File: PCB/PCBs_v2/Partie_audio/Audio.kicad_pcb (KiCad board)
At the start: 2 copper layers, 29.8 x 31.8 mm, 24 parts, among them J1 Conn_01x11, J2 Conn_01x02, U1 PTAS2780RYAR

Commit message: MAJ PCB audio
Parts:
- J1: value Conn_01x11 -> Conn_01x13; footprint Connector_PinHeader_2.00mm:PinHeader_1x11_P2.00mm_Vertical -> Connector_PinHeader_2.00mm:PinHeader_1x13_P2.00mm_Vertical
- moved C2 10.3 mm to (193.6, 39.0)
- moved R1 2.31 mm to (191.6, 46.2)
- moved R2 1.91 mm to (191.0, 43.5), turned to 180 degrees
- moved C4 1.74 mm to (188.5, 48.8)
- moved C10 0.90 mm to (184.8, 40.6)
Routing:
- net GND: track 76.6 -> 12.6 mm, vias 77 -> 74
- net VSNSN: track 19.2 -> 15.4 mm
- net VSNSP: track 17.2 -> 14.0 mm
- net OUTN: track 24.5 -> 21.4 mm
- net /VSNSP_: track 11.1 -> 9.06 mm
- net /VSNSN_: track 4.96 -> 6.78 mm
- net SDIN: track 18.7 -> 16.9 mm
- net SDA: track 15.7 -> 13.9 mm
- net OUTP: track 7.52 -> 9.27 mm
- net /BST_N: track 3.96 -> 5.35 mm
- net +1.8V: track 26.2 -> 27.3 mm
- net /DREG: track 2.84 -> 3.74 mm
- net SBCLK: track 17.6 -> 16.9 mm

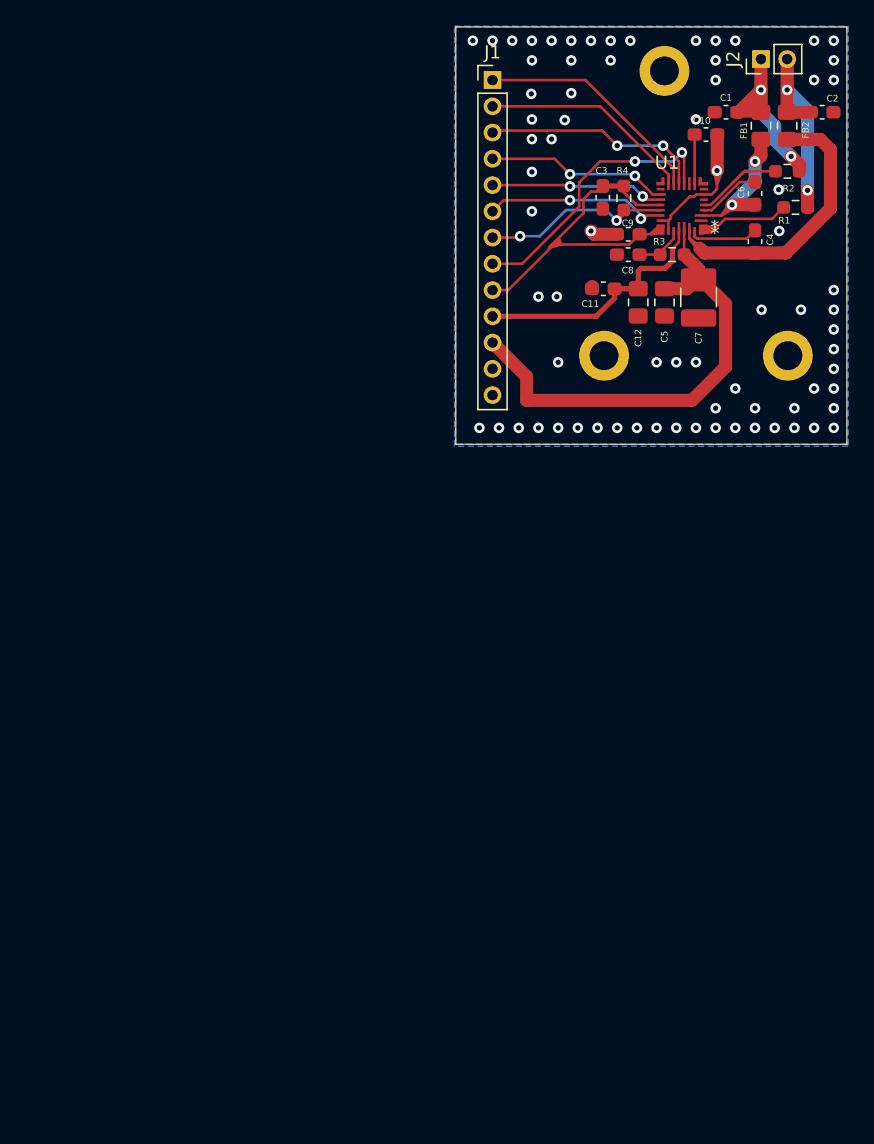
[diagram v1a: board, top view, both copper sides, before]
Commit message: Modification du schéma et du routage de la partie audio
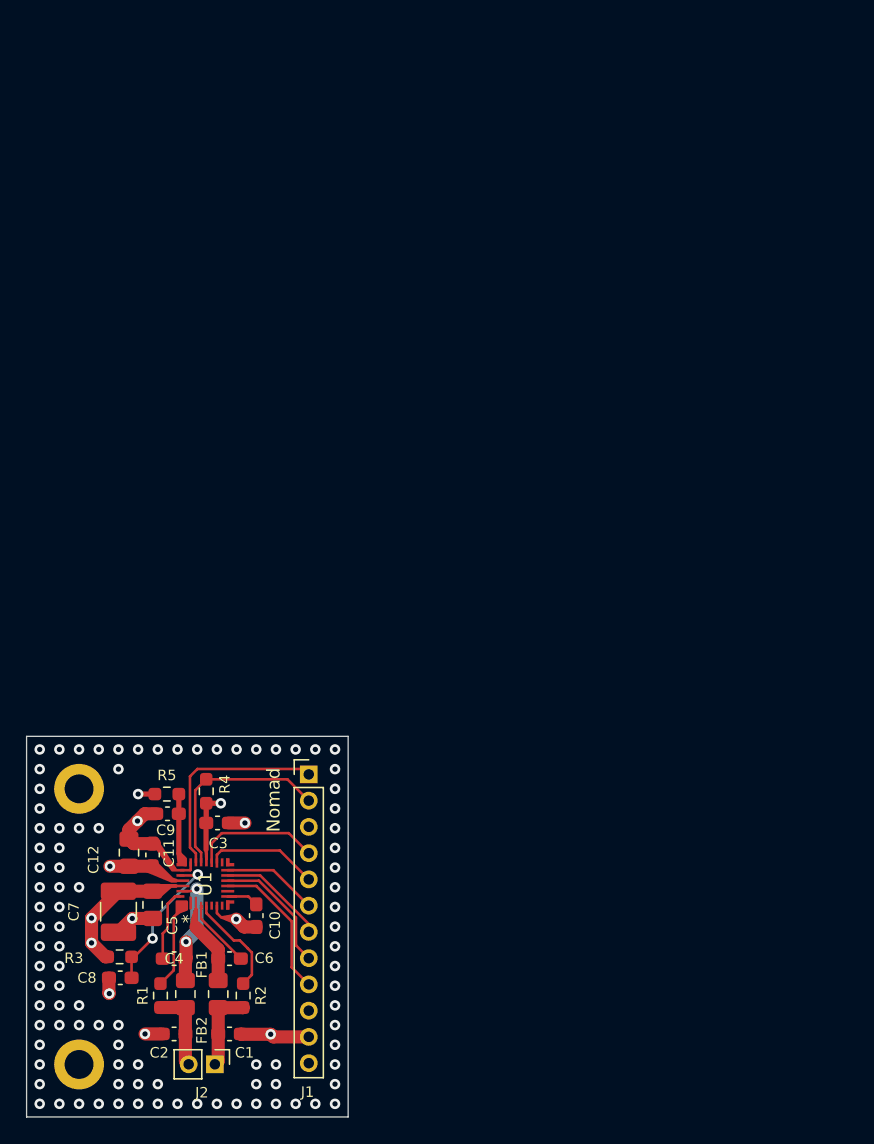
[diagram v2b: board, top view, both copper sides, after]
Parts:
- removed H3: MountingHole_Pad, MountingHole:MountingHole_2.2mm_M2_DIN965_Pad
- added R5: 0, Resistor_SMD:R_0603_1608Metric_Pad0.98x0.95mm_HandSolder, F.Cu at (143.7, 90.9)
- J1: value Conn_01x13 -> Conn_01x12; footprint Connector_PinHeader_2.00mm:PinHeader_1x13_P2.00mm_Vertical -> Connector_PinHeader_2.00mm:PinHeader_1x12_P2.00mm_Vertical
- moved J2 87.2 mm to (147.3, 111.5), turned to -90 degrees
- moved C2 85.8 mm to (144.2, 109.2), turned to 180 degrees
- moved FB2 80.5 mm to (145.1, 106.1), turned to -90 degrees
- moved C1 79.8 mm to (148.5, 109.2), turned to 180 degrees
- moved FB1 78.0 mm to (147.6, 106.1), turned to -90 degrees
- moved R1 77.1 mm to (143.2, 106.2), turned to 90 degrees
- moved H2 76.4 mm to (137.0, 111.5)
- moved R2 75.3 mm to (149.5, 106.2), turned to 90 degrees
- moved C6 70.7 mm to (148.5, 103.4), turned to 0 degrees
- moved H1 70.6 mm to (137.0, 90.5)
- moved C4 70.3 mm to (144.2, 103.4), turned to 0 degrees
- moved C10 68.7 mm to (150.5, 100.2), turned to -90 degrees
- moved R3 68.1 mm to (140.1, 103.3), turned to 180 degrees
- moved C8 67.3 mm to (140.1, 104.9)
- moved C7 64.4 mm to (140.0, 99.9)
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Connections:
- net +5V renamed VBAT1S
- net /VSNSN_ renamed /VSNSN
- net /VSNSP_ renamed /VSNSP
- net VSNSN renamed HP_N
- net VSNSP renamed HP_P
- C3 pad 1: +1.8V -> IOVDD
- C5 pad 1: +12V -> PVDD
- C7 pad 1: +12V -> PVDD
- C9 pad 1: +1.8V -> AVDD
- J1 pad 1: FSYNC -> SDZ
- J1 pad 11: +12V -> GND
- J1 pad 12: GND -> PVDD
- J1 pad 2: SBCLK -> IRQZ
- J1 pad 3: SDIN -> IOVDD
- J1 pad 4: SCL -> SDA
- J1 pad 5: SDA -> SCL
- J1 pad 6: SDZ -> SBCLK
- J1 pad 7: IRQZ -> FSYNC
- J1 pad 8: SDOUT -> SDIN
- J1 pad 9: +1.8V -> SDOUT
- R3 pad 2: +12V -> PVDD
- R4 pad 1: +1.8V -> IOVDD
- U1 pad 20: +1.8V -> IOVDD
- U1 pad 24: +1.8V -> AVDD
- U1 pad 28: +12V -> PVDD
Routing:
- net +12V: track 36.6 -> 0.00 mm
- net +1.8V: track 27.3 -> 0.00 mm
- net VBAT1S: track 19.3 -> 3.25 mm, vias 0 -> 1
- net OUTN: track 21.4 -> 8.52 mm, vias 0 -> 2
- net SDOUT: track 22.1 -> 11.3 mm, vias 2 -> 0
- net SBCLK: track 16.9 -> 7.29 mm
- net FSYNC: track 17.8 -> 8.31 mm
- net GND: track 12.6 -> 21.8 mm, vias 74 -> 102
- net HP_N: track 15.4 -> 6.32 mm, vias 2 -> 0
- net PVDD: track 0.00 -> 9.05 mm, vias 0 -> 2
- net /PVDD_SNS: track 3.80 -> 11.5 mm, vias 0 -> 2
- net HP_P: track 14.0 -> 6.32 mm, vias 2 -> 0
- net SDIN: track 16.9 -> 9.85 mm, vias 2 -> 0
- net IOVDD: track 0.00 -> 6.54 mm, vias 0 -> 2
- net SCL: track 14.0 -> 8.67 mm, vias 2 -> 0
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- added copper zone on In1.Cu, net GND
- added copper zone on In2.Cu, net IOVDD
- added copper zone on In2.Cu, net PVDD
- added copper zone on In2.Cu, net VBAT1S
- removed copper zone on B.Cu, net GND
- removed copper zone on F.Cu, net GND
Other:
- board size 29.8 x 31.8 mm -> 24.5 x 29 mm
- copper layers 2 -> 4
- board text added: "*"
- board text added: "Nomad"

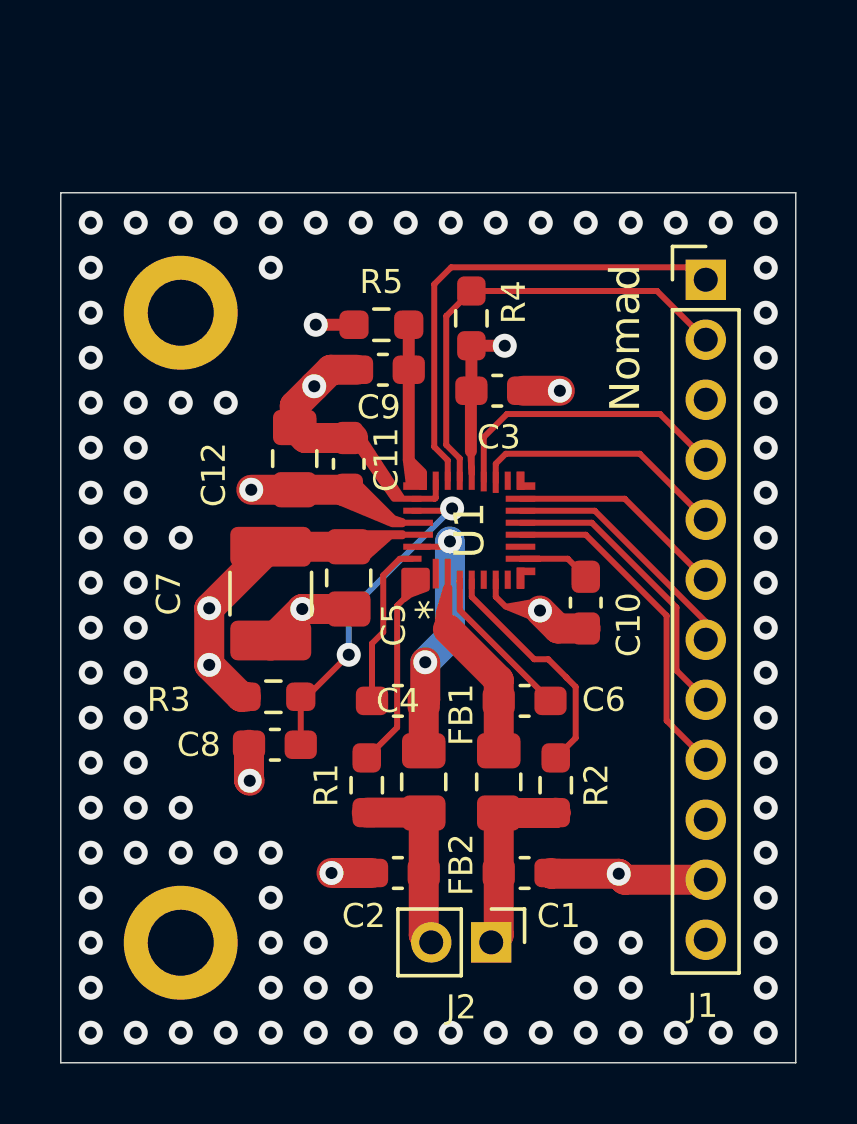
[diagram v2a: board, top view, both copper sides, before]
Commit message: Modification du PCB audio pour avoir un connecteur de 14 broches
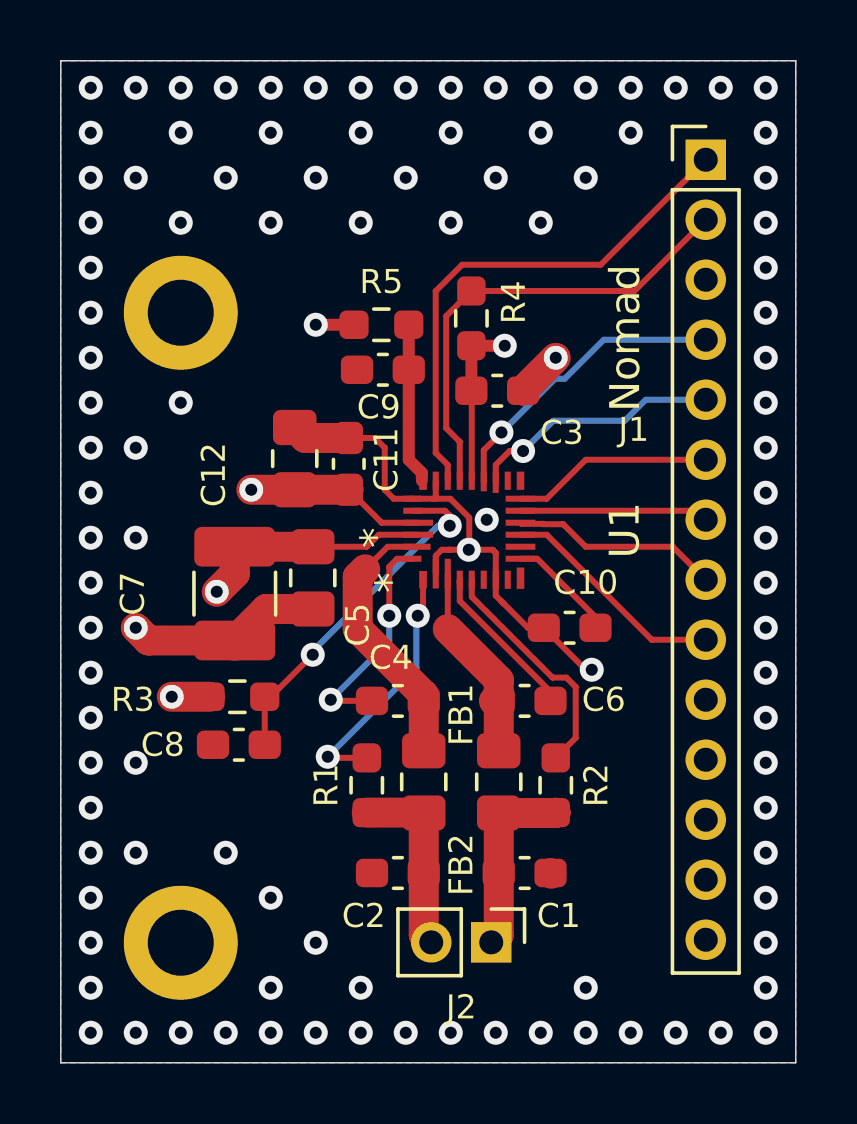
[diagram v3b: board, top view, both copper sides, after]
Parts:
- J1: value Conn_01x12 -> Conn_01x14; footprint Connector_PinHeader_2.00mm:PinHeader_1x12_P2.00mm_Vertical -> Connector_PinHeader_2.00mm:PinHeader_1x14_P2.00mm_Vertical
- moved J1 4.00 mm to (154.5, 85.4)
- moved R3 1.20 mm to (138.9, 103.3)
- moved C5 1.20 mm to (141.4, 99.3)
- moved C7 1.20 mm to (138.8, 99.9)
- moved C8 1.20 mm to (138.9, 104.9)
- moved C10 1.00 mm to (150.0, 101.0), turned to 180 degrees
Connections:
- J1 pad 12: PVDD -> GND
- U1 pad 2: GNDPWR -> GND
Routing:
- net GND: track 21.8 -> 27.0 mm, vias 102 -> 105
- net SDOUT: track 11.3 -> 7.62 mm
- net SDIN: track 9.85 -> 6.97 mm
- net VBAT1S: track 3.25 -> 6.02 mm
- net /VSNSN: track 6.08 -> 8.53 mm, vias 0 -> 2
- net OUTP: track 4.76 -> 6.77 mm
- net FSYNC: track 8.31 -> 6.30 mm
- net /BST_N: track 5.54 -> 7.51 mm, vias 0 -> 2
- net SDZ: track 16.2 -> 17.3 mm
- net AVDD: track 4.50 -> 5.38 mm
- net /DREG: track 3.05 -> 3.79 mm
- net OUTN: track 8.52 -> 9.10 mm, vias 2 -> 0
- net SBCLK: track 7.29 -> 6.71 mm
- net SCL: track 8.67 -> 8.48 mm, vias 0 -> 1
- net SDA: track 9.83 -> 9.99 mm, vias 0 -> 1
- added copper zone on B.Cu, net GND
- added copper zone on F.Cu, net GND
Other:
- board size 24.5 x 29 mm -> 24.5 x 33.4 mm
